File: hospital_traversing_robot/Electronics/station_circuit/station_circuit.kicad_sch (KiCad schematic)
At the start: 17 parts, among them J1 Barrel_Jack_MountingPin, SW1 SW_Nidec_CAS-120A1, U1 Pico, U2 NRF24L01_Breakout, U3 LM338T

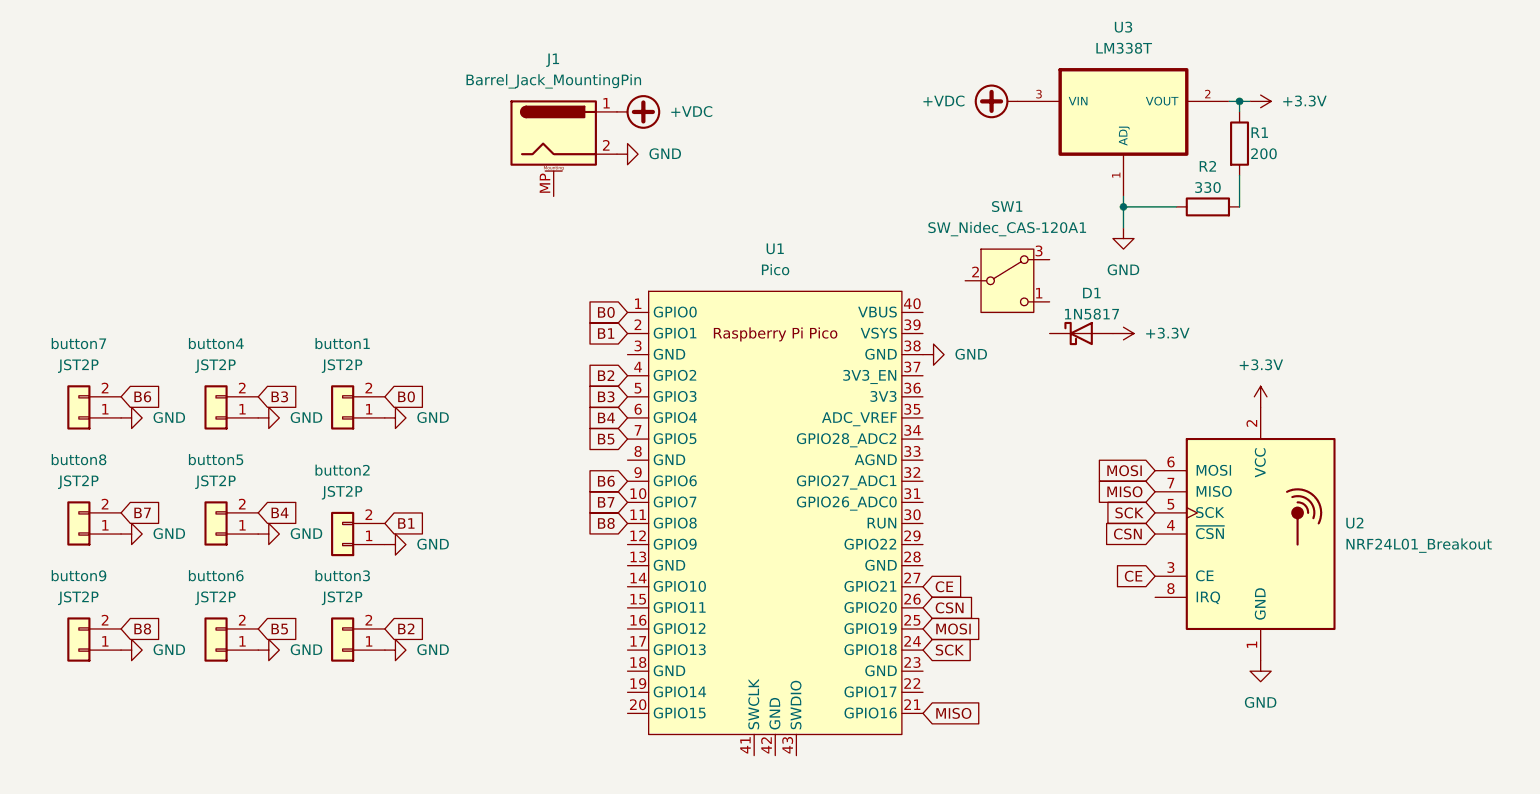
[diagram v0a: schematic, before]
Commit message: finished station circuit PCB and started V2 product display stepper speaker circuit
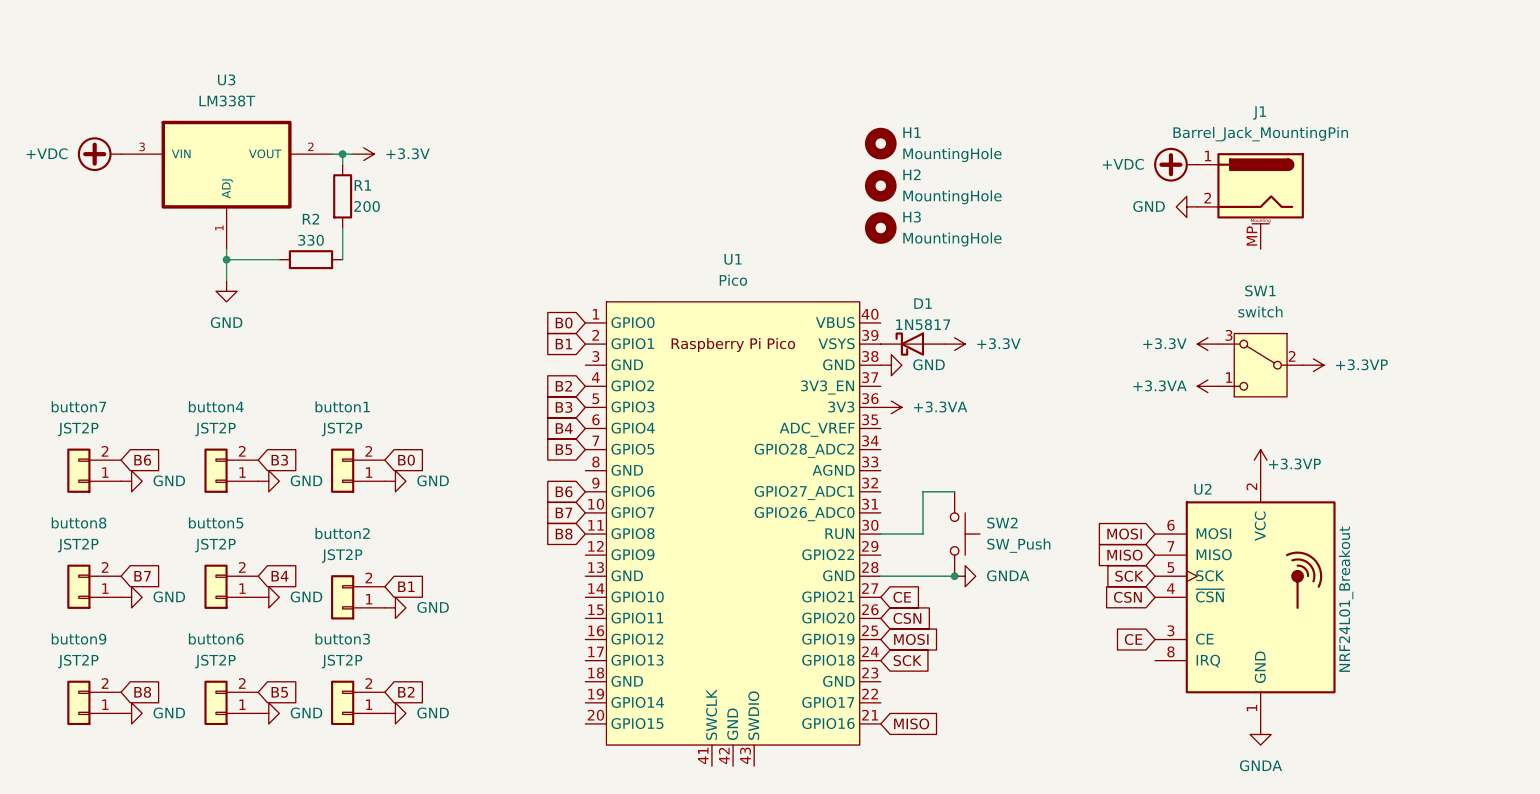
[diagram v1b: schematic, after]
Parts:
- added H1, H2, H3: MountingHole, MountingHole:MountingHole_3.2mm_M3, symbol Mechanical:MountingHole
- added SW2: SW_Push, Button_Switch_THT:SW_PUSH_6mm, symbol Switch:SW_Push
- SW1: value SW_Nidec_CAS-120A1 -> switch; footprint Button_Switch_SMD:Nidec_Copal_CAS-120A -> Connector_PinHeader_2.54mm:PinHeader_1x03_P2.54mm_Vertical
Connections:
- net +3.3V: now also SW1.3 (A); no longer U2.2 (VCC)
- net GND: no longer U2.1 (GND)
- net GNDA: now reaches U1.28 (GND)
- net GNDA: now also U2.1 (GND), SW2.2
- net at U1.30 (RUN): now also SW2.1
- net +3.3VA: now reaches U1.36 (3V3)
- net +3.3VA: now also SW1.1 (C)
- net at U1.39 (VSYS): now also D1.1 (K)
- net +3.3VP: now reaches SW1.2 (B)
- net +3.3VP: now also U2.2 (VCC)
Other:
- moved on the sheet: D1, J1, R1, R2, SW1, U1, U2, U3, button1, button2, button3, button4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
